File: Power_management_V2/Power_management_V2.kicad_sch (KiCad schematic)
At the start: 1 part

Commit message: Hoan thanh SCH mach Power
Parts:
- added J1: Conn_01x03, symbol Connector_Generic:Conn_01x03
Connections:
- net GND: now also J1.3 (Pin_3)
- new net +12V: J1.2 (Pin_2)
- new net +5V: J1.1 (Pin_1)
- no-connect marks 4 -> 2
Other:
- added sheet 12V (12V.kicad_sch)
- sheet 5V ports: added none; removed EN, P_GOOD
- note added: "5V 50W Max"
- note added: "VBat to 12V Buck A Peak 15A Nom. SiC437AED-T1-GE3"
- note added: "VBat to 5V Buck 14A Peak 10A Nom. SiC437AED-T1-GE3"
- note removed: "12V 180W Max"
- note removed: "Reel Motor 9.72A Peak 2.5A Nom. SiC437"

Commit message: Hoan thanh SCH lan 1
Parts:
- J1: value Conn_01x03 -> 02519031301
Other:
- note added: "VBat to 12V Buck A Peak 15A Nom. SIC431AED-T1-GE3"
- note removed: "Mating Connector TE Connectivity 103956-1 DK: A28392-ND Use 22-24 AWG wire"
- note removed: "Mating Contact Molex Ultra-Fit 1722536012 DK: 900-1722536012CT-ND"
- note removed: "Mating Housing Molex Ultra-Fit 1722563102 DK: WM26332-ND"
- note removed: "Mating Housing Molex Ultra-Fit 1722563102 DK:WM26332-ND N.B Polarity difference to 12V con."
- note removed: "VBat to 12V Buck A Peak 15A Nom. SiC437AED-T1-GE3"
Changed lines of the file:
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@@
 		(comment 3 "BAT1, Lidar1, Winch1 connectors updated")
 	)
-	(text "Mating Connector\nTE Connectivity\n103956-1\nDK: A28392-ND\nUse 22-24 AWG wire"
-		(exclude_from_sim no)
-		(at 255.905 46.99 0)
+	(text "Milwaukee 18V\n5S LiPo pack\n21V-16V"
+		(exclude_from_sim no)
+		(at 79.375 28.575 0)
 		(effects
 			(font
@@
 		)
 	)
-	(text "Milwaukee 18V\n5S LiPo pack\n21V-16V"
-		(exclude_from_sim no)
-		(at 20.32 26.67 0)
-		(effects
-			(font
-				(size 1.27 1.27)
-			)
-			(justify left bottom)
-		)
-	)
-	(text "Mating Connector\nTE Connectivity\n103956-1\nDK: A28392-ND\nUse 22-24 AWG wire"
-		(exclude_from_sim no)
-		(at 255.905 74.93 0)
-		(effects
-			(font
-				(size 1.27 1.27)
-			)
-			(justify left bottom)
-		)
-	)
-	(text "Mating Housing\nMolex Ultra-Fit\n1722563102\nDK: WM26332-ND"
-		(exclude_from_sim no)
-		(at 257.175 123.19 0)
-		(effects
-			(font
-				(size 1.27 1.27)
-			)
-			(justify left bottom)
-		)
-	)
-	(text "Mating Housing\nMolex Ultra-Fit\n1722563102\nDK: WM26332-ND"
-		(exclude_from_sim no)
-		(at 255.905 152.4 0)
-		(effects
-			(font
-				(size 1.27 1.27)
-			)
-			(justify left bottom)
-		)
-	)
 	(text "16V Minimum Voltage\n250W Peak draw\n15.6A peak\n"
 		(exclude_from_sim no)
-		(at 20.32 35.56 0)
-		(effects
-			(font
-				(size 1.27 1.27)
-			)
-			(justify left bottom)
-		)
-	)
-	(text "Mating Contact\nMolex Ultra-Fit \n1722536012\nDK: 900-1722536012CT-ND"
-		(exclude_from_sim no)
-		(at 257.175 133.35 0)
+		(at 79.375 37.465 0)
 		(effects
 			(font
@@
 		)
 	)
-	(text "Mating Contact\nMolex Ultra-Fit \n1722536012\nDK: 900-1722536012CT-ND"
-		(exclude_from_sim no)
-		(at 83.82 39.37 0)
-		(effects
-			(font
-				(size 1.27 1.27)
-			)
-			(justify left bottom)
-		)
-	)
-	(text "Mating Contact\nMolex Ultra-Fit \n1722536012\nDK: 900-1722536012CT-ND"
-		(exclude_from_sim no)
-		(at 255.905 162.56 0)
-		(effects
-			(font
-				(size 1.27 1.27)
-			)
-			(justify left bottom)
-		)
-	)
-	(text "Mating Housing\nMolex Ultra-Fit\n1722563102\nDK:WM26332-ND\nN.B Polarity difference to 12V con."
-		(exclude_from_sim no)
-		(at 83.82 29.21 0)
-		(effects
-			(font
-				(size 1.27 1.27)
-			)
-			(justify left bottom)
-		)
-	)
 	(text "VBat to 5V Buck\n14A Peak\n10A Nom.\nSiC437AED-T1-GE3"
 		(exclude_from_sim no)
@@
 		)
 	)
-	(text "Mating Connector\nTE Connectivity\n103956-1\nDK: A28392-ND\nUse 22-24 AWG wire"
-		(exclude_from_sim no)
-		(at 255.905 100.33 0)
-		(effects
-			(font
-				(size 1.27 1.27)
-			)
-			(justify left bottom)
-		)
-	)
-	(text "VBat to 12V Buck\nA Peak\n15A Nom.\nSiC437AED-T1-GE3"
+	(text "VBat to 12V Buck\nA Peak\n15A Nom.\nSIC431AED-T1-GE3"
 		(exclude_from_sim no)
 		(at 50.165 111.125 0)
@@
 	(wire
 		(pts
-			(xy 94.615 66.04) (xy 94.615 85.09)
-		)
-		(stroke
-			(width 0)
-			(type default)
-		)
-	)
-	(wire
-		(pts
-			(xy 94.615 85.09) (xy 109.22 85.09)
+			(xy 81.915 66.04) (xy 81.915 85.09)
+		)
+		(stroke
+			(width 0)
+			(type default)
+		)
+	)
+	(wire
+		(pts
+			(xy 81.915 85.09) (xy 109.22 85.09)
 		)
 		(stroke
@@
 	(wire
 		(pts
-			(xy 72.39 66.04) (xy 94.615 66.04)
+			(xy 72.39 66.04) (xy 81.915 66.04)
 		)
 		(stroke
@@
 		(dnp no)
 		(fields_autoplaced yes)
-		(property "Reference" "#PWR02"
+		(property "Reference" "#PWR04"
 			(at 57.15 43.18 0)
 			(effects
@@
 			(project "power_management"
 				(path "/632966f8-0e72-49d8-ae31-468f807051b0"
-					(reference "#PWR02")
+					(reference "#PWR04")
 					(unit 1)
 				)
@@
 		(on_board yes)
 		(dnp no)
-		(property "Reference" "#PWR01"
+		(property "Reference" "#PWR03"
 			(at 57.15 30.48 0)
 			(effects
@@
 		(property "Description" ""
 			(at 57.15 26.67 0)
+			(effects
+				(font
+					(size 1.27 1.27)
+				)
+			)
+		)
+		(pin "1"
+		)
+		(instances
+			(project "power_management"
+				(path "/632966f8-0e72-49d8-ae31-468f807051b0"
+					(reference "#PWR03")
+					(unit 1)
+				)
+			)
+		)
+	)
+	(symbol
+		(lib_id "power:+BATT")
+		(at 44.45 67.31 0)
+		(unit 1)
+		(exclude_from_sim no)
+		(in_bom yes)
+		(on_board yes)
+		(dnp no)
+		(fields_autoplaced yes)
+		(property "Reference" "#PWR01"
+			(at 44.45 71.12 0)
+			(effects
+				(font
+					(size 1.27 1.27)
+				)
+				(hide yes)
+			)
+		)
+		(property "Value" "+BATT"
+			(at 44.45 63.7342 0)
+			(effects
+				(font
+					(size 1.27 1.27)
+				)
+			)
+		)
+		(property "Footprint" ""
+			(at 44.45 67.31 0)
+			(effects
+				(font
+					(size 1.27 1.27)
+				)
+				(hide yes)
+			)
+		)
+		(property "Datasheet" ""
+			(at 44.45 67.31 0)
+			(effects
+				(font
+					(size 1.27 1.27)
+				)
+				(hide yes)
+			)
+		)
+		(property "Description" ""
+			(at 44.45 67.31 0)
 			(effects
 				(font
@@
 	(symbol
 		(lib_id "power:+BATT")
-		(at 44.45 67.31 0)
+		(at 44.45 113.665 0)
 		(unit 1)
 		(exclude_from_sim no)
@@
 		(dnp no)
 		(fields_autoplaced yes)
-		(property "Reference" "#PWR0101"
-			(at 44.45 71.12 0)
-			(effects
-				(font
-					(size 1.27 1.27)
-				)
-				(hide yes)
-			)
-		)
-		(property "Value" "+BATT"
-			(at 44.45 63.7342 0)
-			(effects
-				(font
-					(size 1.27 1.27)
-				)
-			)
-		)
-		(property "Footprint" ""
-			(at 44.45 67.31 0)
-			(effects
-				(font
-					(size 1.27 1.27)
-				)
-				(hide yes)
-			)
-		)
-		(property "Datasheet" ""
-			(at 44.45 67.31 0)
-			(effects
-				(font
-					(size 1.27 1.27)
-				)
-				(hide yes)
-			)
-		)
-		(property "Description" ""
-			(at 44.45 67.31 0)
-			(effects
-				(font
-					(size 1.27 1.27)
-				)
-			)
-		)
-		(pin "1"
-		)
-		(instances
-			(project "power_management"
-				(path "/632966f8-0e72-49d8-ae31-468f807051b0"
-					(reference "#PWR0101")
-					(unit 1)
-				)
-			)
-		)
-	)
-	(symbol
-		(lib_id "power:+BATT")
-		(at 44.45 113.665 0)
-		(unit 1)
-		(exclude_from_sim no)
-		(in_bom yes)
-		(on_board yes)
-		(dnp no)
-		(fields_autoplaced yes)
-		(property "Reference" "#PWR03"
+		(property "Reference" "#PWR02"
 			(at 44.45 117.475 0)
 			(effects
@@
 			(project "Power_management_V2"
 				(path "/632966f8-0e72-49d8-ae31-468f807051b0"
-					(reference "#PWR03")
+					(reference "#PWR02")
 					(unit 1)
 				)
@@
 			)
 		)
-		(property "Value" "Conn_01x03"
+		(property "Value" "02519031301"
 			(at 116.84 88.8999 0)
 			(effects
@@
 		(dnp no)
 		(fields_autoplaced yes)
-		(property "Reference" "#PWR010"
+		(property "Reference" "#PWR05"
 			(at 106.68 97.79 0)
 			(effects
@@
 			(project "Power_management_V2"
 				(path "/632966f8-0e72-49d8-ae31-468f807051b0"
-					(reference "#PWR010")
+					(reference "#PWR05")
 					(unit 1)
 				)

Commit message: Chỉnh sủa SCH 24/12
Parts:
- added C34: 100n/50V/0603, Library:C_0603_1608Metric, symbol Device:C
- added R15: 2M/0603, Library:R_0603_1608Metric, symbol Device:R
- added R16: 51.1K/0603, Library:R_0603_1608Metric, symbol Device:R
- added R8: 100k/0603, Library:R_0603_1608Metric, symbol Device:R
- added U3: TPS3711DDCR, symbol New_Library:TPS3711DDCR
- J1: value 02519031301 -> 640388-3
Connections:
- net +BATT: now also C34.2, R15.2, R8.2, U3.5 (VDD)
- net GND: now also C34.1, R16.1, U3.2 (GND-2), U3.4 (GND-4), U3.6 (GND-6)
- new net: R15.1, R16.2, U3.3 (SENSE)
- new net 12V/EN_12V: R8.1, U3.1 (OUT)
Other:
- sheet 12V ports: added EN_12V; removed none
- sheet 5V ports: added EN_5V; removed none
- note added: "Imax: 14.4A Pitch:3.96mm"
- note added: "UVLO Protection"
- note added: "UVLO: 16V Vit-=0.4V"
- note added: "VBat to 12V Buck 18A Peak 12A Nom. SIC437AED-T1-GE3"
- note added: "When VBat falls below 16 V, the OUT pin of U3 is asserted low, pulling the EN pins of the 5 V buck converter and the 12 V buck converter to GND, thereby disabling both converters."
- note removed: "VBat to 12V Buck A Peak 15A Nom. SIC431AED-T1-GE3"
- company: Raw Matter IO Pty Ltd -> (none)
- title: Diptek 5S LiPo Power distribution  -> Diptek Power Board V2
- moved on the sheet: J1

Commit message: Hoan thanh footprint
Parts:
- BAT1: footprint Library:CONN02_1723103302_MOL -> Library:Milwaukee 18V battery connector R1
- C34: footprint Library:C_0603_1608Metric -> Capacitor_SMD:C_0603_1608Metric
- J1: footprint (none) -> Library:TE_640388-3
- R15, R16, R8: footprint Library:R_0603_1608Metric -> Resistor_SMD:R_0603_1608Metric
- U3: footprint (none) -> Package_TO_SOT_SMD:TSOT-23-6
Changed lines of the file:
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@@
 			"XPl8OedSirPKV7he7/tB4EJMNE0zTdMwDE8aCV6o67pxHFOySsynq7X2fe/RyldIKbVte/v9Cx+t"
 			"AgC4nZ0JACBETAAAIWICAAgREwBAiJgAAELEBAAQIiYAgBAxAQCEiAkAIERMAAAhYgIACPkFNXKe"
-			"EFKOwUIAAAAASUVORK5CYII="
+			"EFKOwUIAAAAASUVORK5CYIIAAAAAAAAAAAAAAAAAAAAAAAAAAAAAAAAAAAAAAAAAAAAAAAAAAAAA"
+			"AAAAAAAAAAAAAAAAAAAAAAAAAAAAAAAAAAAAAAAAAAAAAAAAAAAAAAAAAAAAAAAAAAAAAAAAAAAA"
+			"AAAAAAAAAAAAAAAAAAAAAAAAAAAAAAAAAAAAAAAAAAAAAAAAAAAAAAAAAAAAAAAAAAAAAAAAAAAA"
+			"AAAAAAAAAAAAAAAAAAAAAAAAAAAAAAAAAAAAAAAAAAAAAAAAAAAAAAAAAAAAAAAAAAAAAAAAAAAA"
+			"AAAAAAAAAAAAAAAAAAAAAAAAAAAAAAAAAAAAAAAAAAAAAAAAAAAAAAAAAAAAAAAAAAAAAAAAAAAA"
+			"AAAAAAAAAAAAAAAAAAAAAAAAAAAAAAAAAAAAAAAAAAAAAAAAAAAAAAAAAAAAAAAAAAAAAAAAAAAA"
+			"AAAAAAAAAAAAAAAAAAAAAAAAAAAAAAAAAAAAAAAAAAAAAAAAAAAAAAAAAAAAAAAAAAAAAAAAAAAA"
+			"AAAAAAAAAAAAAAAAAAAAAAAAAAAAAAAAAAAAAAAAAAAAAAAAAAAAAAAAAAAAAAAAAAAAAAAAAAAA"
+			"AAAAAAAAAAAAAAAAAAAAAAAAAAAAAAAAAAAAAAAAAAAAAAAAAAAAAAAAAAAAAAAAAAAAAAAAAAAA"
+			"AAAAAAAAAAAAAAAAAAAAAAAAAAAAAAAAAAAAAAAAAAAAAAAAAAAAAAAAAAAAAAAAAAAAAAAAAAAA"
+			"AAAAAAAAAAAAAAAAAAAAAAAAAAAAAAAAAAAAAAAAAAAAAAAAAAAAAAAAAAAAAAAAAAAAAAAAAAAA"
+			"AAAAAAAAAAAAAAAAAAAAAAAAAAAAAAAAAAAAAAAAAAAAAAAAAAAAAAAAAAAAAAAAAAAAAAAAAAAA"
+			"AAAAAAAAAAAAAAAAAAAAAAAAAAAAAAAAAAAAAAAAAAAAAAAAAAAAAAAAAAAAAAAAAAAAAAAAAAAA"
+			"AAAAAAAAAAAAAAAAAAAAAAAAAAAAAAAAAAAAAAAAAAAAAAAAAAAAAAAAAAAAAAAAAAAAAAAAAAAA"
+			"AAAAAAAAAAAAAAAAAAAAAAAAAAAAAAAAAAAAAAAAAAAAAAAAAAAAAAAAAAAAAAAAAAAAAAAAAAAA"
+			"AAAAAAAAAAAAAAAAAAAAAAAAAAAAAAAAAAAAAAAAAAAAAAAAAAAAAAAAAAAAAAAAAAAAAAAAAAAA"
+			"AAAAAAAAAAAAAAAAAAAAAAAAAAAAAAAAAAAAAAAAAAAAAAAAAAAAAAAAAAAAAAAAAAAAAAAAAAAA"
+			"AAAAAAAAAAAAAAAAAAAAAAAAAAAAAAAAAAAAAAAAAAAAAAAAAAAAAAAAAAAAAAAAAAAAAAAAAAAA"
+			"AAAAAAAAAAAAAAAAAAAAAA=="
 		)
 	)
@@
 			)
 		)
-		(property "Footprint" "Library:R_0603_1608Metric"
+		(property "Footprint" "Resistor_SMD:R_0603_1608Metric"
 			(at 63.373 99.695 90)
 			(effects
@@
 				)
 				(hide yes)
+			)
+		)
+		(property "Sim.Device" ""
+			(at 61.595 99.695 0)
+			(effects
+				(font
+					(size 1.27 1.27)
+				)
+			)
+		)
+		(property "Sim.Params" ""
+			(at 61.595 99.695 0)
+			(effects
+				(font
+					(size 1.27 1.27)
+				)
+			)
+		)
+		(property "Sim.Pins" ""
+			(at 61.595 99.695 0)
+			(effects
+				(font
+					(size 1.27 1.27)
+				)
 			)
 		)
@@
 			)
 		)
-		(property "Footprint" "Library:R_0603_1608Metric"
+		(property "Footprint" "Resistor_SMD:R_0603_1608Metric"
 			(at 114.173 78.74 90)
 			(effects
@@
 				)
 				(hide yes)
+			)
+		)
+		(property "Sim.Device" ""
+			(at 112.395 78.74 0)
+			(effects
+				(font
+					(size 1.27 1.27)
+				)
+			)
+		)
+		(property "Sim.Params" ""
+			(at 112.395 78.74 0)
+			(effects
+				(font
+					(size 1.27 1.27)
+				)
+			)
+		)
+		(property "Sim.Pins" ""
+			(at 112.395 78.74 0)
+			(effects
+				(font
+					(size 1.27 1.27)
+				)
 			)
 		)
@@
 			)
 		)
-		(property "Footprint" "Library:C_0603_1608Metric"
+		(property "Footprint" "Capacitor_SMD:C_0603_1608Metric"
 			(at 53.0098 74.295 0)
 			(effects
@@
 				)
 				(hide yes)
+			)
+		)
+		(property "Sim.Device" ""
+			(at 53.975 78.105 0)
+			(effects
+				(font
+					(size 1.27 1.27)
+				)
+			)
+		)
+		(property "Sim.Params" ""
+			(at 53.975 78.105 0)
+			(effects
+				(font
+					(size 1.27 1.27)
+				)
+			)
+		)
+		(property "Sim.Pins" ""
+			(at 53.975 78.105 0)
+			(effects
+				(font
+					(size 1.27 1.27)
+				)
 			)
 		)
@@
 			)
 		)
-		(property "Footprint" "Library:CONN02_1723103302_MOL"
+		(property "Footprint" "Library:Milwaukee 18V battery connector R1"
 			(at 63.5 27.94 0)
 			(effects
@@
 				)
 				(hide yes)
+			)
+		)
+		(property "Sim.Device" ""
+			(at 63.5 27.94 0)
+			(effects
+				(font
+					(size 1.27 1.27)
+				)
+			)
+		)
+		(property "Sim.Params" ""
+			(at 63.5 27.94 0)
+			(effects
+				(font
+					(size 1.27 1.27)
+				)
+			)
+		)
+		(property "Sim.Pins" ""
+			(at 63.5 27.94 0)
+			(effects
+				(font
+					(size 1.27 1.27)
+				)
 			)
 		)
@@
 			)
 		)
-		(property "Footprint" ""
+		(property "Footprint" "Library:TE_640388-3"
 			(at 230.505 91.44 0)
 			(effects
@@
 				)
 				(hide yes)
+			)
+		)
+		(property "Sim.Device" ""
+			(at 230.505 91.44 0)
+			(effects
+				(font
+					(size 1.27 1.27)
+				)
+			)
+		)
+		(property "Sim.Params" ""
+			(at 230.505 91.44 0)
+			(effects
+				(font
+					(size 1.27 1.27)
+				)
+			)
+		)
+		(property "Sim.Pins" ""
+			(at 230.505 91.44 0)
+			(effects
+				(font
+					(size 1.27 1.27)
+				)
 			)
 		)
@@
 			)
 		)
-		(property "Footprint" ""
+		(property "Footprint" "Package_TO_SOT_SMD:TSOT-23-6"
 			(at 84.455 93.345 0)
 			(effects
@@
 				)
 				(hide yes)
+			)
+		)
+		(property "Sim.Device" ""
+			(at 84.455 93.345 0)
+			(effects
+				(font
+					(size 1.27 1.27)
+				)
+			)
+		)
+		(property "Sim.Params" ""
+			(at 84.455 93.345 0)
+			(effects
+				(font
+					(size 1.27 1.27)
+				)
+			)
+		)
+		(property "Sim.Pins" ""
+			(at 84.455 93.345 0)
+			(effects
+				(font
+					(size 1.27 1.27)
+				)
 			)
 		)
@@
 			)
 		)
-		(property "Footprint" "Library:R_0603_1608Metric"
+		(property "Footprint" "Resistor_SMD:R_0603_1608Metric"
 			(at 63.373 90.805 90)
 			(effects
@@
 			)
 		)
+		(property "Sim.Device" ""
+			(at 61.595 90.805 0)
+			(effects
+				(font
+					(size 1.27 1.27)
+				)
+			)
+		)
+		(property "Sim.Params" ""
+			(at 61.595 90.805 0)
+			(effects
+				(font
+					(size 1.27 1.27)
+				)
+			)
+		)
+		(property "Sim.Pins" ""
+			(at 61.595 90.805 0)
+			(effects
+				(font
+					(size 1.27 1.27)
+				)
+			)
+		)

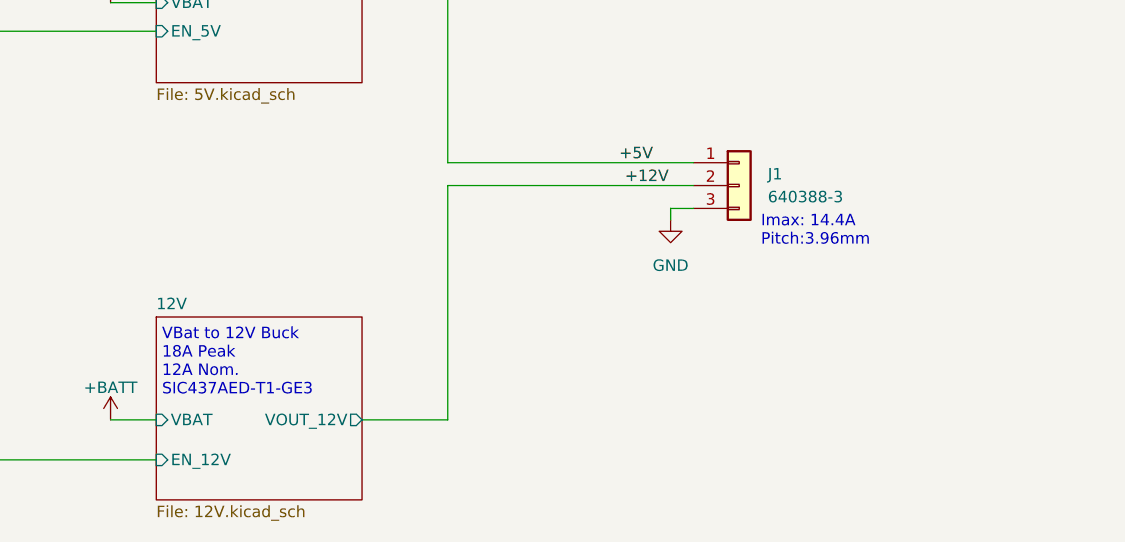
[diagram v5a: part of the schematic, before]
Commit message: Cập nhật connecter 12 5
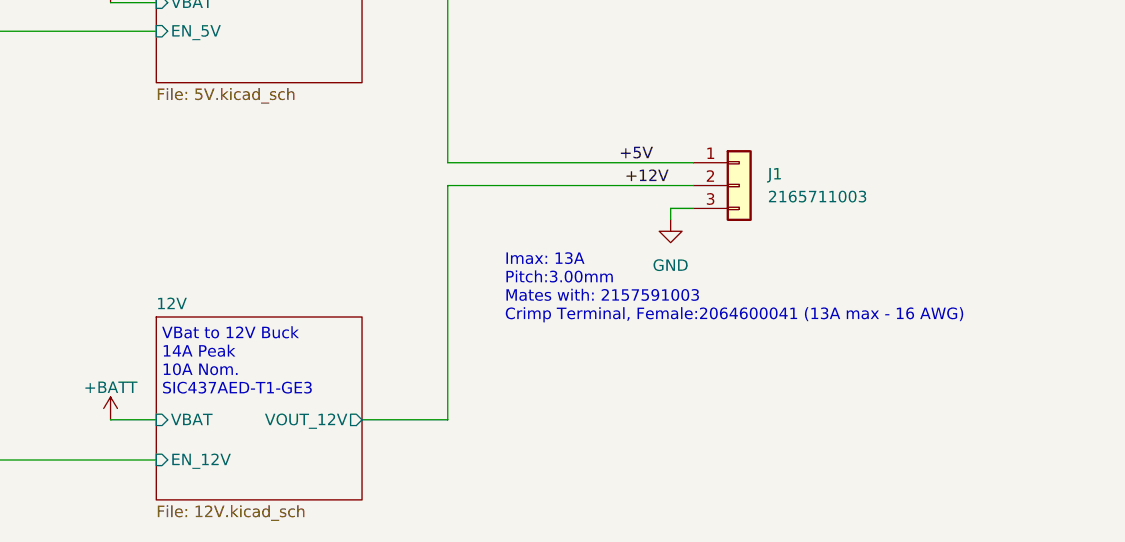
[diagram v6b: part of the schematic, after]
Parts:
- J1: value 640388-3 -> 2165711003; footprint Library:TE_640388-3 -> Library:MOLEX_2165711003
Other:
- note added: "Imax: 13A Pitch:3.00mm Mates with: 2157591003 Crimp Terminal, Female:2064600041 (13A max - 16 AWG)"
- note added: "VBat to 12V Buck 14A Peak 10A Nom. SIC437AED-T1-GE3"
- note removed: "Imax: 14.4A Pitch:3.96mm"
- note removed: "VBat to 12V Buck 18A Peak 12A Nom. SIC437AED-T1-GE3"
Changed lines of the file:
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@@
 		)
 	)
-	(text "Imax: 14.4A\nPitch:3.96mm"
+	(text "Imax: 13A\nPitch:3.00mm\nMates with: 2157591003 \nCrimp Terminal, Female:2064600041 (13A max - 16 AWG)"
 		(exclude_from_sim no)
-		(at 232.918 98.298 0)
+		(at 204.47 106.68 0)
 		(effects
 			(font
@@
 		)
 	)
-	(text "VBat to 12V Buck\n18A Peak\n12A Nom.\nSIC437AED-T1-GE3"
+	(text "VBat to 12V Buck\n14A Peak\n10A Nom.\nSIC437AED-T1-GE3"
 		(exclude_from_sim no)
 		(at 166.37 114.935 0)
@@
 			"AAAAAAAAAAAAAAAAAAAAAAAAAAAAAAAAAAAAAAAAAAAAAAAAAAAAAAAAAAAAAAAAAAAAAAAAAAAA"
 			"AAAAAAAAAAAAAAAAAAAAAAAAAAAAAAAAAAAAAAAAAAAAAAAAAAAAAAAAAAAAAAAAAAAAAAAAAAAA"
+			"AAAAAAAAAAAAAAAAAAAAAAAAAAAAAAAAAAAAAAAAAAAAAAAAAAAAAAAAAAAAAAAAAAAAAAAAAAAA"
+			"AAAAAAAAAAAAAAAAAAAAAAAAAAAAAAAAAAAAAAAAAAAAAAAAAAAAAAAAAAAAAAAAAAAAAAAAAAAA"
+			"AAAAAAAAAAAAAAAAAAAAAAAAAAAAAAAAAAAAAAAAAAAAAAAAAAAAAAAAAAAAAAAAAAAAAAAAAAAA"
+			"AAAAAAAAAAAAAAAAAAAAAAAAAAAAAAAAAAAAAAAAAAAAAAAAAAAAAAAAAAAAAAAAAAAAAAAAAAAA"
+			"AAAAAAAAAAAAAAAAAAAAAAAAAAAAAAAAAAAAAAAAAAAAAAAAAAAAAAAAAAAAAAAAAAAAAAAAAAAA"
+			"AAAAAAAAAAAAAAAAAAAAAAAAAAAAAAAAAAAAAAAAAAAAAAAAAAAAAAAAAAAAAAAAAAAAAAAAAAAA"
+			"AAAAAAAAAAAAAAAAAAAAAAAAAAAAAAAAAAAAAAAAAAAAAAAAAAAAAAAAAAAAAAAAAAAAAAAAAAAA"
+			"AAAAAAAAAAAAAAAAAAAAAAAAAAAAAAAAAAAAAAAAAAAAAAAAAAAAAAAAAAAAAAAAAAAAAAAAAAAA"
+			"AAAAAAAAAAAAAAAAAAAAAAAAAAAAAAAAAAAAAAAAAAAAAAAAAAAAAAAAAAAAAAAAAAAAAAAAAAAA"
+			"AAAAAAAAAAAAAAAAAAAAAAAAAAAAAAAAAAAAAAAAAAAAAAAAAAAAAAAAAAAAAAAAAAAAAAAAAAAA"
+			"AAAAAAAAAAAAAAAAAAAAAAAAAAAAAAAAAAAAAAAAAAAAAAAAAAAAAAAAAAAAAAAAAAAAAAAAAAAA"
+			"AAAAAAAAAAAAAAAAAAAAAAAAAAAAAAAAAAAAAAAAAAAAAAAAAAAAAAAAAAAAAAAAAAAAAAAAAAAA"
+			"AAAAAAAAAAAAAAAAAAAAAAAAAAAAAAAAAAAAAAAAAAAAAAAAAAAAAAAAAAAAAAAAAAAAAAAAAAAA"
+			"AAAAAAAAAAAAAAAAAAAAAAAAAAAAAAAAAAAAAAAAAAAAAAAAAAAAAAAAAAAAAAAAAAAAAAAAAAAA"
+			"AAAAAAAAAAAAAAAAAAAAAAAAAAAAAAAAAAAAAAAAAAAAAAAAAAAAAAAAAAAAAAAAAAAAAAAAAAAA"
+			"AAAAAAAAAAAAAAAAAAAAAAAAAAAAAAAAAAAAAAAAAAAAAAAAAAAAAAAAAAAAAAAAAAAAAAAAAAAA"
+			"AAAAAAAAAAAAAAAAAAAAAAAAAAAAAAAAAAAAAAAAAAAAAAAAAAAAAAAAAAAAAAAAAAAAAAAAAAAA"
+			"AAAAAAAAAAAAAAAAAAAAAAAAAAAAAAAAAAAAAAAAAAAAAAAAAAAAAAAAAAAAAAAAAAAAAAAAAAAA"
+			"AAAAAAAAAAAAAAAAAAAAAAAAAAAAAAAAAAAAAAAAAAAAAAAAAAAAAAAAAAAAAAAAAAAAAAAAAAAA"
+			"AAAAAAAAAAAAAAAAAAAAAAAAAAAAAAAAAAAAAAAAAAAAAAAAAAAAAAAAAAAAAAAAAAAAAAAAAAAA"
+			"AAAAAAAAAAAAAAAAAAAAAAAAAAAAAAAAAAAAAAAAAAAAAAAAAAAAAAAAAAAAAAAAAAAAAAAAAAAA"
+			"AAAAAAAAAAAAAAAAAAAAAAAAAAAAAAAAAAAAAAAAAAAAAAAAAAAAAAAAAAAAAAAAAAAAAAAAAAAA"
+			"AAAAAAAAAAAAAAAAAAAAAAAAAAAAAAAAAAAAAAAAAAAAAAAAAAAAAAAAAAAAAAAAAAAAAAAAAAAA"
+			"AAAAAAAAAAAAAAAAAAAAAAAAAAAAAAAAAAAAAAAAAAAAAAAAAAAAAAAAAAAAAAAAAAAAAAAAAAAA"
+			"AAAAAAAAAAAAAAAAAAAAAAAAAAAAAAAAAAAAAAAAAAAAAAAAAAAAAAAAAAAAAAAAAAAAAAAAAAAA"
+			"AAAAAAAAAAAAAAAAAAAAAAAAAAAAAAAAAAAAAAAAAAAAAAAAAAAAAAAAAAAAAAAAAAAAAAAAAAAA"
+			"AAAAAAAAAAAAAAAAAAAAAAAAAAAAAAAAAAAAAAAAAAAAAAAAAAAAAAAAAAAAAAAAAAAAAAAAAAAA"
+			"AAAAAAAAAAAAAAAAAAAAAAAAAAAAAAAAAAAAAAAAAAAAAAAAAAAAAAAAAAAAAAAAAAAAAAAAAAAA"
+			"AAAAAAAAAAAAAAAAAAAAAAAAAAAAAAAAAAAAAAAAAAAAAAAAAAAAAAAAAAAAAAAAAAAAAAAAAAAA"
+			"AAAAAAAAAAAAAAAAAAAAAAAAAAAAAAAAAAAAAAAAAAAAAAAAAAAAAAAAAAAAAAAAAAAAAAAAAAAA"
+			"AAAAAAAAAAAAAAAAAAAAAAAAAAAAAAAAAAAAAAAAAAAAAAAAAAAAAAAAAAAAAAAAAAAAAAAAAAAA"
+			"AAAAAAAAAAAAAAAAAAAAAAAAAAAAAAAAAAAAAAAAAAAAAAAAAAAAAAAAAAAAAAAAAAAAAAAAAAAA"
+			"AAAAAAAAAAAAAAAAAAAAAAAAAAAAAAAAAAAAAAAAAAAAAAAAAAAAAAAAAAAAAAAAAAAAAAAAAAAA"
+			"AAAAAAAAAAAAAAAAAAAAAAAAAAAAAAAAAAAAAAAAAAAAAAAAAAAAAAAAAAAAAAAAAAAAAAAAAAAA"
+			"AAAAAAAAAAAAAAAAAAAAAAAAAAAAAAAAAAAAAAAAAAAAAAAAAAAAAAAAAAAAAAAAAAAAAAAAAAAA"
+			"AAAAAAAAAAAAAAAAAAAAAAAAAAAAAAAAAAAAAAAAAAAAAAAAAAAAAAAAAAAAAAAAAAAAAAAAAAAA"
 			"AAAAAAAAAAAAAAAAAAAAAA=="
 		)
@@
 			)
 		)
-		(property "Value" "640388-3"
+		(property "Value" "2165711003"
 			(at 233.68 92.7099 0)
 			(effects
@@
 			)
 		)
-		(property "Footprint" "Library:TE_640388-3"
+		(property "Footprint" "Library:MOLEX_2165711003"
 			(at 230.505 91.44 0)
 			(effects
